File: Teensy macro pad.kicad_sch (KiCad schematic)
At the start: 47 parts, among them J1 USB_C_Receptacle_USB2.0_14P, J2 AVR-ISP-6, J3 Conn_01x05_Pin, SW0,0 CherryMX, SW0,1 CherryMX, SW0,2 CherryMX, SW0,3 CherryMX, SW0,4 CherryMX, SW1 SW_Push, SW1,0 CherryMX, SW1,1 CherryMX, SW1,2 CherryMX, SW1,3 CherryMX, SW1,4 CherryMX, SW2,0 CherryMX, SW2,1 CherryMX, SW2,2 CherryMX, SW2,3 CherryMX, SW2,4 CherryMX, SW3,0 CherryMX, SW3,1 CherryMX, SW3,2 CherryMX, SW3,3 CherryMX, SW3,4 CherryMX, U1 ATmega32U4-A, Y1 16 MHz

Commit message: Add holes for bridge pins on the switches
The switches I intend to use for the project have two extra pins in the
bottom corners, which are simply bridged together. Rather than cut them
off, it seems like a good opportunity to try customizing a footprint, so
create a modified footprint which adds holes for the pins. The Cherry MX
datasheet [0] provided pin locations and recommended hole dimensions.

[0]: https://cdn.sparkfun.com/datasheets/Components/Switches/MX%20Series.pdf
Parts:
- SW0,0, SW0,1, SW0,2, SW0,3, SW0,4, SW1,0, SW1,1, SW1,2, SW1,3, SW1,4, SW2,0, SW2,1, SW2,2, SW2,3, SW2,4, SW3,0, SW3,1, SW3,2, SW3,3, SW3,4: footprint Button_Switch_Keyboard:SW_Cherry_MX_1.00u_PCB -> CherryMX with bridge:SW_Cherry_MX_1.00u_PCB_with_bridge
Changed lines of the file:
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@@
 			)
 		)
-		(property "Footprint" "Button_Switch_Keyboard:SW_Cherry_MX_1.00u_PCB"
+		(property "Footprint" "CherryMX with bridge:SW_Cherry_MX_1.00u_PCB_with_bridge"
 			(at 243.84 17.145 0)
 			(effects
@@
 			)
 		)
-		(property "Footprint" "Button_Switch_Keyboard:SW_Cherry_MX_1.00u_PCB"
+		(property "Footprint" "CherryMX with bridge:SW_Cherry_MX_1.00u_PCB_with_bridge"
 			(at 243.84 61.595 0)
 			(effects
@@
 			)
 		)
-		(property "Footprint" "Button_Switch_Keyboard:SW_Cherry_MX_1.00u_PCB"
+		(property "Footprint" "CherryMX with bridge:SW_Cherry_MX_1.00u_PCB_with_bridge"
 			(at 243.84 118.745 0)
 			(effects
@@
 			)
 		)
-		(property "Footprint" "Button_Switch_Keyboard:SW_Cherry_MX_1.00u_PCB"
+		(property "Footprint" "CherryMX with bridge:SW_Cherry_MX_1.00u_PCB_with_bridge"
 			(at 243.84 150.495 0)
 			(effects
@@
 			)
 		)
-		(property "Footprint" "Button_Switch_Keyboard:SW_Cherry_MX_1.00u_PCB"
+		(property "Footprint" "CherryMX with bridge:SW_Cherry_MX_1.00u_PCB_with_bridge"
 			(at 243.84 36.195 0)
 			(effects
@@
 			)
 		)
-		(property "Footprint" "Button_Switch_Keyboard:SW_Cherry_MX_1.00u_PCB"
+		(property "Footprint" "CherryMX with bridge:SW_Cherry_MX_1.00u_PCB_with_bridge"
 			(at 243.84 106.045 0)
 			(effects
@@
 			)
 		)
-		(property "Footprint" "Button_Switch_Keyboard:SW_Cherry_MX_1.00u_PCB"
+		(property "Footprint" "CherryMX with bridge:SW_Cherry_MX_1.00u_PCB_with_bridge"
 			(at 243.84 112.395 0)
 			(effects
@@
 			)
 		)
-		(property "Footprint" "Button_Switch_Keyboard:SW_Cherry_MX_1.00u_PCB"
+		(property "Footprint" "CherryMX with bridge:SW_Cherry_MX_1.00u_PCB_with_bridge"
 			(at 243.84 67.945 0)
 			(effects
@@
 			)
 		)
-		(property "Footprint" "Button_Switch_Keyboard:SW_Cherry_MX_1.00u_PCB"
+		(property "Footprint" "CherryMX with bridge:SW_Cherry_MX_1.00u_PCB_with_bridge"
 			(at 243.84 74.295 0)
 			(effects
@@
 			)
 		)
-		(property "Footprint" "Button_Switch_Keyboard:SW_Cherry_MX_1.00u_PCB"
+		(property "Footprint" "CherryMX with bridge:SW_Cherry_MX_1.00u_PCB_with_bridge"
 			(at 243.84 99.695 0)
 			(effects
@@
 			)
 		)
-		(property "Footprint" "Button_Switch_Keyboard:SW_Cherry_MX_1.00u_PCB"
+		(property "Footprint" "CherryMX with bridge:SW_Cherry_MX_1.00u_PCB_with_bridge"
 			(at 243.84 131.445 0)
 			(effects
@@
 			)
 		)
-		(property "Footprint" "Button_Switch_Keyboard:SW_Cherry_MX_1.00u_PCB"
+		(property "Footprint" "CherryMX with bridge:SW_Cherry_MX_1.00u_PCB_with_bridge"
 			(at 243.84 29.845 0)
 			(effects
@@
 			)
 		)
-		(property "Footprint" "Button_Switch_Keyboard:SW_Cherry_MX_1.00u_PCB"
+		(property "Footprint" "CherryMX with bridge:SW_Cherry_MX_1.00u_PCB_with_bridge"
 			(at 243.84 93.345 0)
 			(effects
@@
 			)
 		)
-		(property "Footprint" "Button_Switch_Keyboard:SW_Cherry_MX_1.00u_PCB"
+		(property "Footprint" "CherryMX with bridge:SW_Cherry_MX_1.00u_PCB_with_bridge"
 			(at 243.84 144.145 0)
 			(effects
@@
 			)
 		)
-		(property "Footprint" "Button_Switch_Keyboard:SW_Cherry_MX_1.00u_PCB"
+		(property "Footprint" "CherryMX with bridge:SW_Cherry_MX_1.00u_PCB_with_bridge"
 			(at 243.84 137.795 0)
 			(effects
@@
 			)
 		)
-		(property "Footprint" "Button_Switch_Keyboard:SW_Cherry_MX_1.00u_PCB"
+		(property "Footprint" "CherryMX with bridge:SW_Cherry_MX_1.00u_PCB_with_bridge"
 			(at 243.84 23.495 0)
 			(effects
@@
 			)
 		)
-		(property "Footprint" "Button_Switch_Keyboard:SW_Cherry_MX_1.00u_PCB"
+		(property "Footprint" "CherryMX with bridge:SW_Cherry_MX_1.00u_PCB_with_bridge"
 			(at 243.84 80.645 0)
 			(effects
@@
 			)
 		)
-		(property "Footprint" "Button_Switch_Keyboard:SW_Cherry_MX_1.00u_PCB"
+		(property "Footprint" "CherryMX with bridge:SW_Cherry_MX_1.00u_PCB_with_bridge"
 			(at 243.84 55.245 0)
 			(effects
@@
 			)
 		)
-		(property "Footprint" "Button_Switch_Keyboard:SW_Cherry_MX_1.00u_PCB"
+		(property "Footprint" "CherryMX with bridge:SW_Cherry_MX_1.00u_PCB_with_bridge"
 			(at 243.84 156.845 0)
 			(effects
@@
 			)
 		)
-		(property "Footprint" "Button_Switch_Keyboard:SW_Cherry_MX_1.00u_PCB"
+		(property "Footprint" "CherryMX with bridge:SW_Cherry_MX_1.00u_PCB_with_bridge"
 			(at 243.84 42.545 0)
 			(effects

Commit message: Add JLCPCB part numbers
C7 and C8 (10pF capacitors) had to be changed to a smaller 0603
footprint, so that I could use parts on the basic JLCPCB parts list.
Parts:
- C7, C8: footprint Capacitor_SMD:C_0805_2012Metric -> Capacitor_SMD:C_0603_1608Metric
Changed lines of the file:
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@@
 			)
 		)
-		(property "Footprint" "Capacitor_SMD:C_0805_2012Metric"
+		(property "Footprint" "Capacitor_SMD:C_0603_1608Metric"
 			(at 105.1052 25.4 0)
 			(effects
@@
 			)
 		)
-		(property "Footprint" "Capacitor_SMD:C_0805_2012Metric"
+		(property "Footprint" "Capacitor_SMD:C_0603_1608Metric"
 			(at 89.8652 25.4 0)
 			(effects

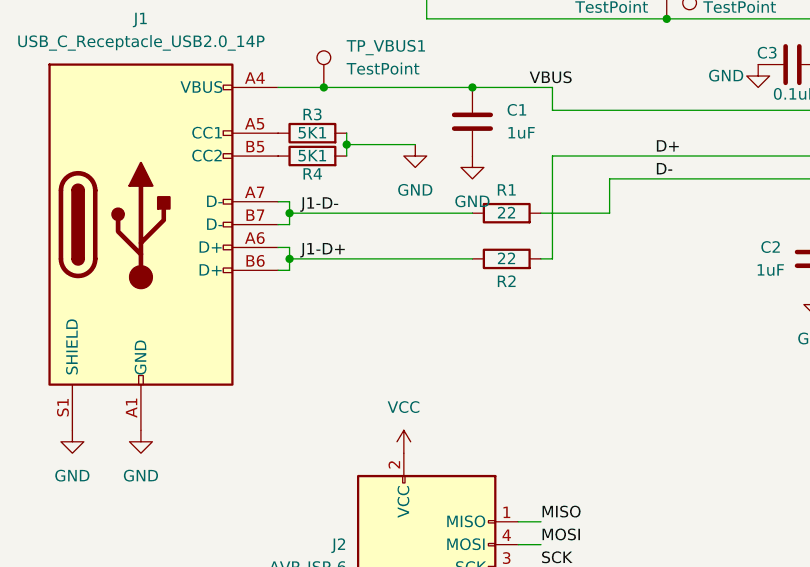
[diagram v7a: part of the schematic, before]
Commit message: Add USB test points
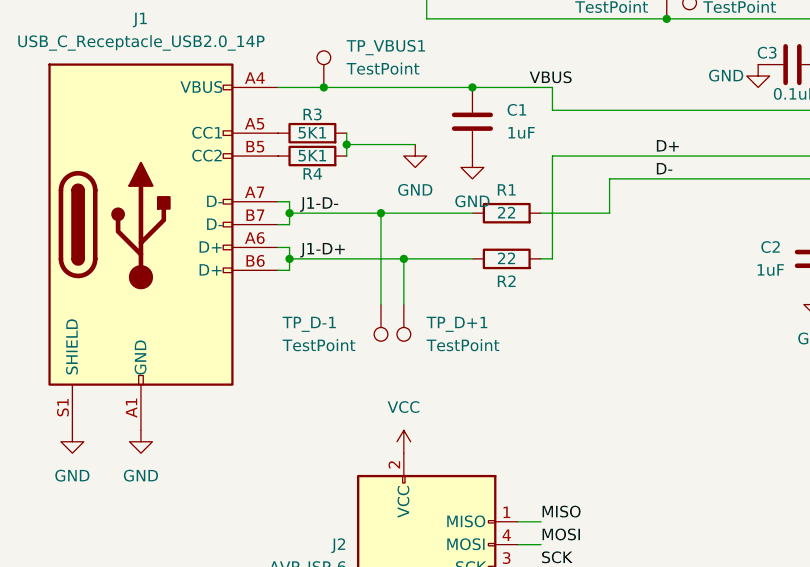
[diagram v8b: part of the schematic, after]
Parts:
- added TP_D+1, TP_D-1: TestPoint, TestPoint:TestPoint_Pad_D2.0mm, symbol Connector:TestPoint
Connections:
- net J1-D+: now also TP_D+1.1
- net J1-D-: now also TP_D-1.1
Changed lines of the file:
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@@
 	)
 	(junction
+		(at 83.82 68.58)
+		(diameter 0)
+		(color 0 0 0 0)
+	)
+	(junction
 		(at 252.73 119.38)
 		(diameter 0)
@@
 	)
 	(junction
+		(at 86.36 73.66)
+		(diameter 0)
+		(color 0 0 0 0)
+	)
+	(junction
 		(at 252.73 113.03)
 		(diameter 0)
@@
 	(wire
 		(pts
+			(xy 83.82 68.58) (xy 83.82 78.74)
+		)
+		(stroke
+			(width 0)
+			(type default)
+		)
+	)
+	(wire
+		(pts
+			(xy 86.36 73.66) (xy 86.36 78.74)
+		)
+		(stroke
+			(width 0)
+			(type default)
+		)
+	)
+	(wire
+		(pts
 			(xy 170.18 34.29) (xy 170.18 41.91)
 		)
@@
 	(wire
 		(pts
-			(xy 73.66 73.66) (xy 93.98 73.66)
+			(xy 73.66 73.66) (xy 86.36 73.66)
 		)
 		(stroke
@@
 	(wire
 		(pts
+			(xy 86.36 73.66) (xy 93.98 73.66)
+		)
+		(stroke
+			(width 0)
+			(type default)
+		)
+	)
+	(wire
+		(pts
 			(xy 101.6 73.66) (xy 102.87 73.66)
 		)
@@
 	(wire
 		(pts
-			(xy 73.66 68.58) (xy 93.98 68.58)
+			(xy 73.66 68.58) (xy 83.82 68.58)
 		)
 		(stroke
@@
 	(wire
 		(pts
+			(xy 83.82 68.58) (xy 93.98 68.58)
+		)
+		(stroke
+			(width 0)
+			(type default)
+		)
+	)
+	(wire
+		(pts
 			(xy 238.76 81.28) (xy 187.96 81.28)
 		)
@@
 	)
 	(symbol
+		(lib_id "Connector:TestPoint")
+		(at 83.82 78.74 180)
+		(unit 1)
+		(exclude_from_sim no)
+		(in_bom yes)
+		(on_board yes)
+		(dnp no)
+		(property "Reference" "TP_D-1"
+			(at 72.898 80.772 0)
+			(effects
+				(font
+					(size 1.27 1.27)
+				)
+				(justify right)
+			)
+		)
+		(property "Value" "TestPoint"
+			(at 72.898 83.312 0)
+			(effects
+				(font
+					(size 1.27 1.27)
+				)
+				(justify right)
+			)
+		)
+		(property "Footprint" "TestPoint:TestPoint_Pad_D2.0mm"
+			(at 78.74 78.74 0)
+			(effects
+				(font
+					(size 1.27 1.27)
+				)
+				(hide yes)
+			)
+		)
+		(property "Datasheet" "~"
+			(at 78.74 78.74 0)
+			(effects
+				(font
+					(size 1.27 1.27)
+				)
+				(hide yes)
+			)
+		)
+		(property "Description" "test point"
+			(at 83.82 78.74 0)
+			(effects
+				(font
+					(size 1.27 1.27)
+				)
+				(hide yes)
+			)
+		)
+		(pin "1"
+		)
+		(instances
+			(project "Teensy macro pad"
+				(path "/bcf4c563-ed90-4192-81fd-782593c0996d"
+					(reference "TP_D-1")
+					(unit 1)
+				)
+			)
+		)
+	)
+	(symbol
 		(lib_id "Device:R")
 		(at 97.79 68.58 90)
@@
 					(unit 1)
 				)
+			)
+		)
+	)
+	(symbol
+		(lib_id "Connector:TestPoint")
+		(at 86.36 78.74 180)
+		(unit 1)
+		(exclude_from_sim no)
+		(in_bom yes)
+		(on_board yes)
+		(dnp no)
+		(fields_autoplaced yes)
+		(property "Reference" "TP_D+1"
+			(at 88.9 80.7719 0)
+			(effects
+				(font
+					(size 1.27 1.27)
+				)
+				(justify right)
+			)
+		)
+		(property "Value" "TestPoint"
+			(at 88.9 83.3119 0)
+			(effects
+				(font
+					(size 1.27 1.27)
+				)
+				(justify right)
+			)
+		)
+		(property "Footprint" "TestPoint:TestPoint_Pad_D2.0mm"
+			(at 81.28 78.74 0)
+			(effects
+				(font
+					(size 1.27 1.27)
+				)
+				(hide yes)
+			)
+		)
+		(property "Datasheet" "~"
+			(at 81.28 78.74 0)
+			(effects
+				(font
+					(size 1.27 1.27)
+				)
+				(hide yes)
+			)
+		)
+		(property "Description" "test point"
+			(at 86.36 78.74 0)
+			(effects
+				(font
+					(size 1.27 1.27)
+				)
+				(hide yes)
+			)
+		)
+		(pin "1"
+		)
+		(instances
+			(project "Teensy macro pad"
+				(path "/bcf4c563-ed90-4192-81fd-782593c0996d"
+					(reference "TP_D+1")
+					(unit 1)
+				)
